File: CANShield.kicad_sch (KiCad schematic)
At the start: 25 parts, among them J1 Conn_01x04_Socket, J2 Conn_02x19_Odd_Even, J3 Conn_02x19_Odd_Even, U1 TJA1443ATK/0Z

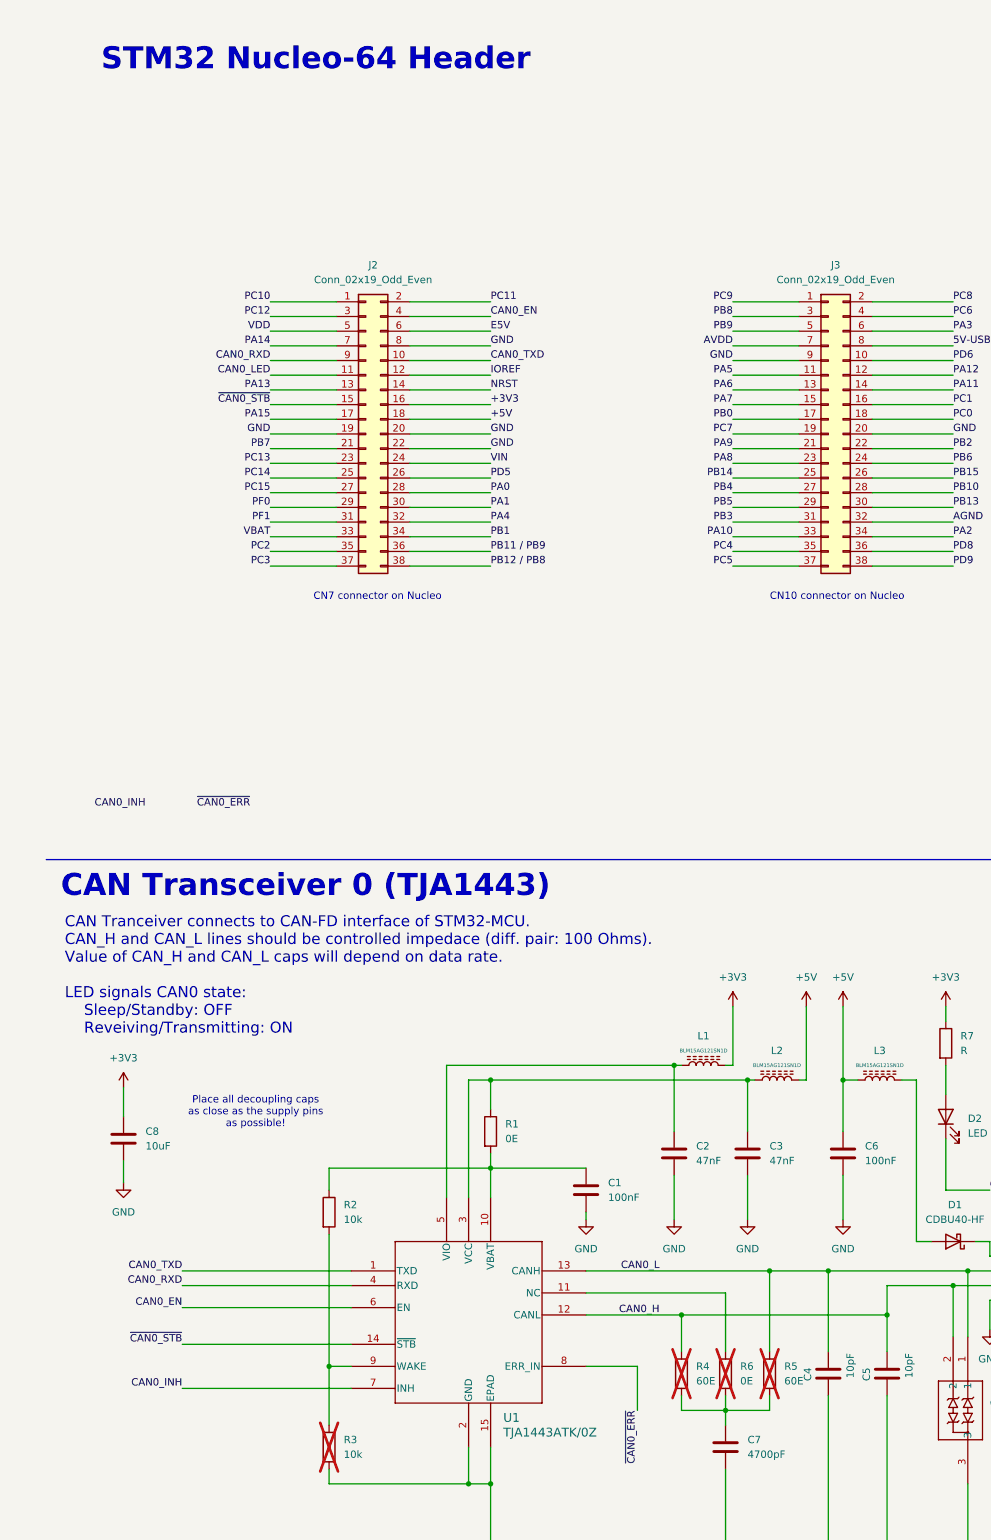
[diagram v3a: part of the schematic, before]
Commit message: Update CANShield.kicad_sch
Add testpoints and documentation
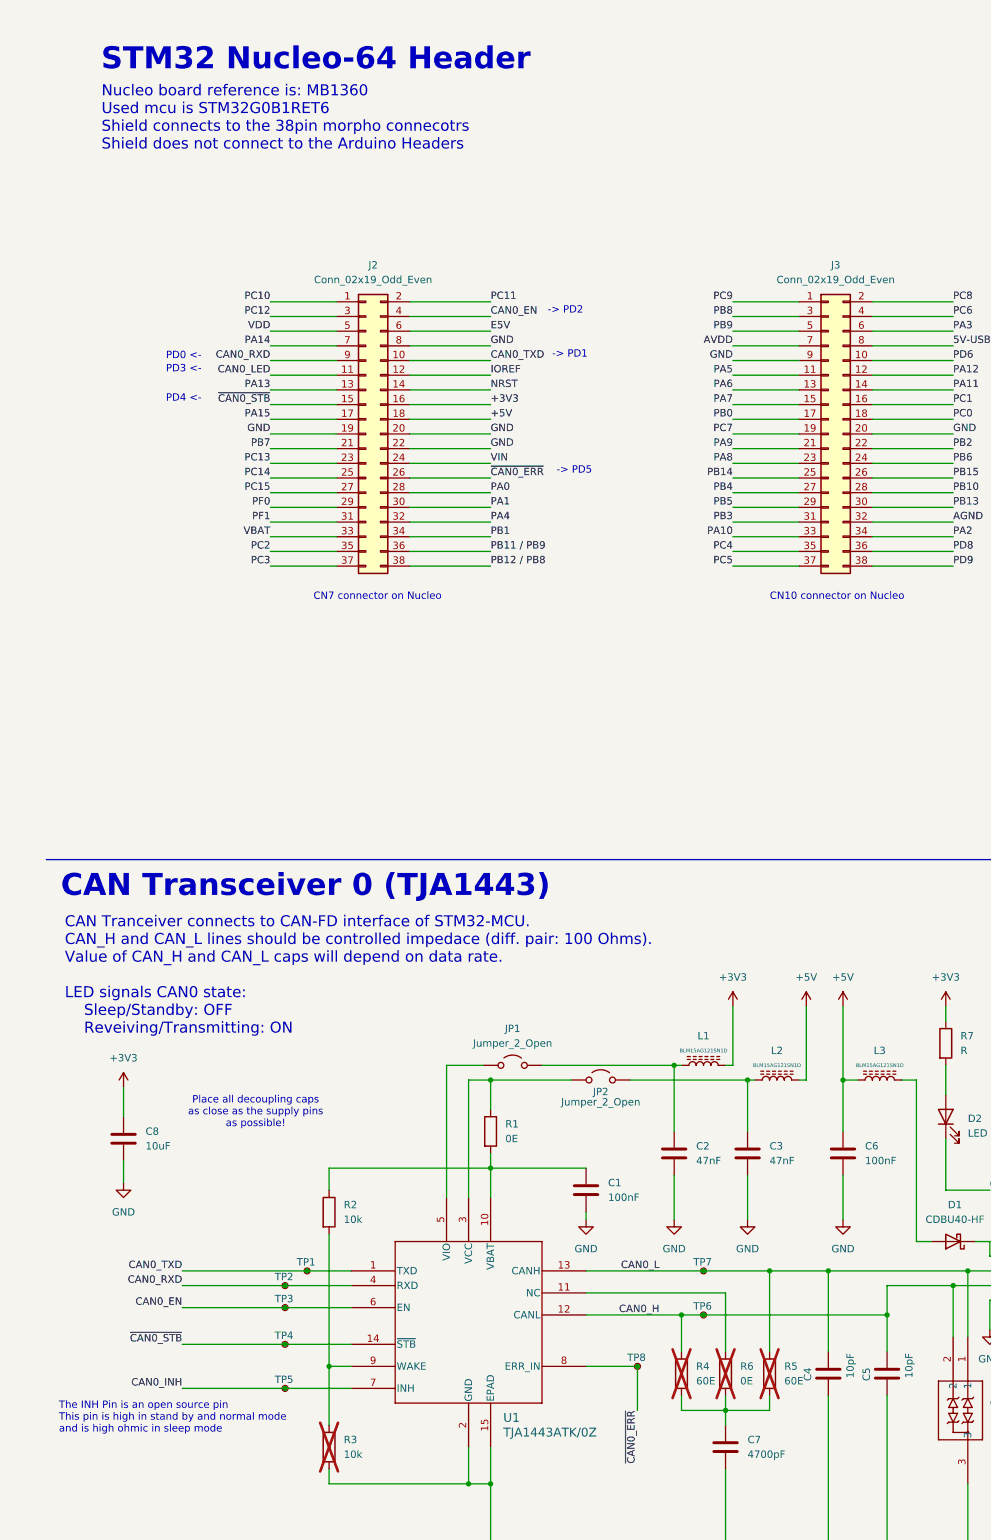
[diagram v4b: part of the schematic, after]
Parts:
- added JP1, JP2: Jumper_2_Open, symbol Jumper:Jumper_2_Open
- added TP1, TP2, TP3, TP4, TP5, TP6, TP7, TP8: TestPoint_Small, symbol Connector:TestPoint_Small
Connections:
- net PD5 is gone; now on net ~{CAN0_ERR}: J2.26 (Pin_26)
- net CAN0_EN: now also TP3.1
- net CAN0_H: now also TP6.1
- net CAN0_INH: now also TP5.1
- net CAN0_L: now also TP7.1
- net CAN0_RXD: now also TP2.1
- net CAN0_TXD: now also TP1.1
- net ~{CAN0_ERR}: now also TP8.1
- net ~{CAN0_STB}: now also TP4.1
- net at R1.1, U1.3 (VCC): now also JP2.1 (A); no longer C3.1, L2.1
- net at C2.1, L1.1: now also JP1.2 (B); no longer U1.5 (VIO)
- new net: JP1.1 (A), U1.5 (VIO)
- new net: C3.1, JP2.2 (B), L2.1
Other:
- note added: "-> PD1"
- note added: "-> PD2"
- note added: "-> PD5"
- note added: "Nucleo board reference is: MB1360 Used mcu is STM32G0B1RET6 Shield connects to the 38pin morpho connecotrs Shield does not connect to the Arduino Headers"
- note added: "PD0 <-"
- note added: "PD3 <-"
- note added: "PD4 <-"
- note added: "The INH Pin is an open source pin This pin is high in stand by and normal mode and is high ohmic in sleep mode"

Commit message: Update CANShield.kicad_sch
Add probe connector and Flash memory
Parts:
- added C10: 120uF, symbol Device:C
- added C11, C13: 100nF, symbol Device:C
- added C12, C9: 10uF, symbol Device:C
- added CR2: PESD2CANFD27V-TR, SOT23_PESD2_NEX, symbol PESD2CANFD27V:PESD2CANFD27V-TR
- added D3: LED_ARGB, symbol Device:LED_ARGB
- added J4: Conn_01x06_Socket, symbol Connector:Conn_01x06_Socket
- added L4, L5, L6, L7: BLM15AG121SN1D, symbol Device:L_Ferrite
- added Q1, Q2, Q3: Si1308EDL, Package_TO_SOT_SMD:SOT-323_SC-70, symbol Transistor_FET:Si1308EDL
- added R10, R14, R15, R16, R17, R18, R19, R20, R8, R9: 100k, symbol Device:R
- added R11, R12, R13: 1k, symbol Device:R
- added U2: AT25SF081-XMHD-X, Package_SO:TSSOP-8_4.4x3mm_P0.65mm, symbol Memory_Flash:AT25SF081-XMHD-X
- added U5: BD2222G, Package_SO:TSOP-6_1.65x3.05mm_P0.95mm, symbol Power_Management:BD2222G
- R7: value R -> 1k
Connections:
- net +3V3: now also C12.1, C13.1, D3.1 (A), R17.1, R19.1, R20.1, U2.8 (VCC)
- net +5V: now also C9.1, U5.1 (IN)
- net GND: now also C10.2, C11.2, C12.2, C13.2, C9.2, CR2.3, L6.1, Q1.2 (S), Q2.2 (S), Q3.2 (S), R10.2, R16.2, R18.2, R8.2, R9.2, U2.4 (GND), U5.2 (GND)
- net PA10 renamed PROBE_EN
- net PROBE_EN: now also R16.1, U5.3 (EN)
- net PA8 renamed FLASH_CS
- net FLASH_CS: now also R19.2, U2.1 (~{CS})
- net PA9 renamed ~{WP}
- net ~{WP}: now also U2.3 (~{WP}/IO2)
- net PB13 renamed SCLK
- net SCLK: now also U2.6 (SCK)
- net PB14 renamed MISO
- net MISO: now also U2.2 (SO/IO1)
- net PB15 renamed MOSI
- net MOSI: now also U2.5 (SI/IO0)
- net PB3 renamed LED0_RED
- net LED0_RED: now also Q1.1 (G), R8.1
- net PB4 renamed LED0_BLU
- net LED0_BLU: now also Q3.1 (G), R10.1
- net PB5 renamed LED0_GRN
- net LED0_GRN: now also Q2.1 (G), R9.1
- net PC4 renamed USART1_TX
- net USART1_TX: now also CR2.1, L4.1, R15.2
- net PC5 renamed USART1_RX
- net USART1_RX: now also CR2.2, L5.1, R14.2
- net PD9 renamed ~{PRB_FLG}
- net ~{PRB_FLG}: now also R17.2, U5.4 (~{OC})
- new net: R18.1, U5.5 (ILIM)
- new net: Q2.3 (D), R12.2
- new net: D3.2 (RK), R11.2
- new net: D3.3 (GK), R12.1
- new net: D3.4 (BK), R13.1
- new net: J4.2 (Pin_2), L6.2
- new net: Q3.3 (D), R13.2
- new net: J4.1 (Pin_1), L7.2
- new net: Q1.3 (D), R11.1
- new net: J4.4 (Pin_4), L4.2
- new net: J4.3 (Pin_3), L5.2
- new net PVCC: C10.1, C11.1, L7.1, R14.1, R15.1, U5.6 (OUT)
- new net ~{HOLD}: R20.2, U2.7 (~{HOLD}/IO3)
- no-connect marks 0 -> 2
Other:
- note added: "-> PB13"
- note added: "-> PB15"
- note added: "-> PD9"
- note added: "8Mbit NOR-Flash Memory to save firmware update"
- note added: "Current limiting probe switch. Probe connector with ESD protection."
- note added: "Flash Memory"
- note added: "LED States: RED: Fatal Error Yellow: In progress Green: Progress successful Magenta: Service Mode Cyan: Open state"
- note added: "PA10 <-"
- note added: "PA8 <-"
- note added: "PA9 <-"
- note added: "PB14 <-"
- note added: "PB3 <-"
- note added: "PB4 <-"
- note added: "PB5 <-"
- note added: "PC4 <-"
- note added: "PC5 <-"
- note added: "Probe Switch"
- note added: "RGB Status LED indicates device state. In Canable Dongle this will be the LED Ring indication"
- note added: "Status indication"

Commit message: Update CANShield.kicad_sch
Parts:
- added C114: 100nF, Capacitor_SMD:C_0402_1005Metric_Pad0.74x0.62mm_HandSolder, symbol Device:C
- added D104: LED_ARGB, 155124M173200:LED_155124M173200, symbol Device:LED_ARGB
- added FID101, FID102, FID103: Fiducial, Fiducial:Fiducial_0.75mm_Mask2.25mm, symbol Mechanical:Fiducial
- added H101, H102, H103: MountingHole, MountingHole:MountingHole_2.7mm_M2.5, symbol Mechanical:MountingHole
- added JP102, JP103: SolderJumper_2_Open, Connector_PinHeader_2.54mm:PinHeader_1x02_P2.54mm_Vertical, symbol Jumper:SolderJumper_2_Open
- added R118, R119, R124, R125, R126: 0E, Resistor_SMD:R_0402_1005Metric_Pad0.72x0.64mm_HandSolder, symbol Device:R
- added R122: 100k, Resistor_SMD:R_0402_1005Metric_Pad0.72x0.64mm_HandSolder, symbol Device:R
- added TP109, TP110, TP111, TP112, TP113, TP114, TP115, TP116, TP117, TP118: TestPoint_Small, TestPoint:TestPoint_Pad_D1.0mm, symbol Connector:TestPoint_Small
- added U104: MR20H40, Package_SO:SOIC-8-1EP_3.9x4.9mm_P1.27mm_EP2.29x3mm, symbol Memory_NVRAM:MR20H40
- C101: renamed from C8; footprint (none) -> Capacitor_SMD:C_0603_1608Metric_Pad1.08x0.95mm_HandSolder
- C102: renamed from C1; footprint (none) -> Capacitor_SMD:C_0402_1005Metric_Pad0.74x0.62mm_HandSolder
- C103: renamed from C2; footprint (none) -> Capacitor_SMD:C_0402_1005Metric_Pad0.74x0.62mm_HandSolder
- C104: renamed from C7; footprint (none) -> Capacitor_SMD:C_0402_1005Metric_Pad0.74x0.62mm_HandSolder
- C105: renamed from C3; footprint (none) -> Capacitor_SMD:C_0402_1005Metric_Pad0.74x0.62mm_HandSolder
- C106: renamed from C4; footprint (none) -> Capacitor_SMD:C_0402_1005Metric_Pad0.74x0.62mm_HandSolder
- C107: renamed from C6; footprint (none) -> Capacitor_SMD:C_0402_1005Metric_Pad0.74x0.62mm_HandSolder
- C108: renamed from C5; footprint (none) -> Capacitor_SMD:C_0402_1005Metric_Pad0.74x0.62mm_HandSolder
- C109: renamed from C12; footprint (none) -> Capacitor_SMD:C_0603_1608Metric_Pad1.08x0.95mm_HandSolder
- C110: renamed from C9; footprint (none) -> Capacitor_SMD:C_0603_1608Metric_Pad1.08x0.95mm_HandSolder
- C111: renamed from C13; footprint (none) -> Capacitor_SMD:C_0402_1005Metric_Pad0.74x0.62mm_HandSolder
- C112: renamed from C10; footprint (none) -> Capacitor_SMD:C_0603_1608Metric_Pad1.08x0.95mm_HandSolder
- C113: renamed from C11; footprint (none) -> Capacitor_SMD:C_0402_1005Metric_Pad0.74x0.62mm_HandSolder
- CR101: renamed from CR1; footprint SOT23_PESD2_NEX -> PESD2CANFD27V-TR:SOT23_PESD2_NEX
- CR102: renamed from CR2; footprint SOT23_PESD2_NEX -> PESD2CANFD27V-TR:SOT23_PESD2_NEX
- D101: renamed from D2; footprint (none) -> LED_SMD:LED_0402_1005Metric_Pad0.77x0.64mm_HandSolder
- D103: renamed from D3; footprint (none) -> 155124M173200:LED_155124M173200
- J101: renamed from J2; footprint (none) -> Connector_PinHeader_2.54mm:PinHeader_2x19_P2.54mm_Vertical
- J102: renamed from J3; footprint (none) -> Connector_PinHeader_2.54mm:PinHeader_2x19_P2.54mm_Vertical
- J103: renamed from J1; footprint (none) -> Connector_PinHeader_2.54mm:PinHeader_1x04_P2.54mm_Horizontal
- J104: renamed from J4; footprint (none) -> Connector_Molex:Molex_PicoBlade_53048-0610_1x06_P1.25mm_Horizontal
- JP101: renamed from JP1; footprint (none) -> Connector_PinHeader_2.54mm:PinHeader_1x02_P2.54mm_Vertical
- JP104: renamed from JP2; footprint (none) -> Connector_PinHeader_2.54mm:PinHeader_1x02_P2.54mm_Vertical
- L101: renamed from L1; footprint (none) -> Inductor_SMD:L_0402_1005Metric_Pad0.77x0.64mm_HandSolder
- L102: renamed from L2; footprint (none) -> Inductor_SMD:L_0402_1005Metric_Pad0.77x0.64mm_HandSolder
- L103: renamed from L3; footprint (none) -> Inductor_SMD:L_0402_1005Metric_Pad0.77x0.64mm_HandSolder
- L104: renamed from L7; footprint (none) -> Inductor_SMD:L_0402_1005Metric_Pad0.77x0.64mm_HandSolder
- L105: renamed from L6; footprint (none) -> Inductor_SMD:L_0402_1005Metric_Pad0.77x0.64mm_HandSolder
- L106: renamed from L5; footprint (none) -> Inductor_SMD:L_0402_1005Metric_Pad0.77x0.64mm_HandSolder
- L107: renamed from L4; footprint (none) -> Inductor_SMD:L_0402_1005Metric_Pad0.77x0.64mm_HandSolder
- R101: renamed from R2; footprint (none) -> Resistor_SMD:R_0402_1005Metric_Pad0.72x0.64mm_HandSolder
- R102: renamed from R3; footprint (none) -> Resistor_SMD:R_0402_1005Metric_Pad0.72x0.64mm_HandSolder
- R103: renamed from R1; footprint (none) -> Resistor_SMD:R_0402_1005Metric_Pad0.72x0.64mm_HandSolder
- R104: renamed from R4; footprint (none) -> Resistor_SMD:R_0603_1608Metric_Pad0.98x0.95mm_HandSolder
- R105: renamed from R6; footprint (none) -> Resistor_SMD:R_0603_1608Metric_Pad0.98x0.95mm_HandSolder
- R106: renamed from R5; footprint (none) -> Resistor_SMD:R_0603_1608Metric_Pad0.98x0.95mm_HandSolder
- R107: renamed from R7; footprint (none) -> Resistor_SMD:R_0402_1005Metric_Pad0.72x0.64mm_HandSolder
- R108: renamed from R16; footprint (none) -> Resistor_SMD:R_0402_1005Metric_Pad0.72x0.64mm_HandSolder
- R109: renamed from R8; footprint (none) -> Resistor_SMD:R_0402_1005Metric_Pad0.72x0.64mm_HandSolder
- R110: renamed from R11; footprint (none) -> Resistor_SMD:R_0402_1005Metric_Pad0.72x0.64mm_HandSolder
- R111: renamed from R17; footprint (none) -> Resistor_SMD:R_0402_1005Metric_Pad0.72x0.64mm_HandSolder
- R112: renamed from R19; footprint (none) -> Resistor_SMD:R_0402_1005Metric_Pad0.72x0.64mm_HandSolder
- R113: renamed from R18; footprint (none) -> Resistor_SMD:R_0402_1005Metric_Pad0.72x0.64mm_HandSolder
- R114: renamed from R9; footprint (none) -> Resistor_SMD:R_0402_1005Metric_Pad0.72x0.64mm_HandSolder
- R115: renamed from R20; footprint (none) -> Resistor_SMD:R_0402_1005Metric_Pad0.72x0.64mm_HandSolder
- R116: renamed from R12; footprint (none) -> Resistor_SMD:R_0402_1005Metric_Pad0.72x0.64mm_HandSolder
- R117: renamed from R15; footprint (none) -> Resistor_SMD:R_0402_1005Metric_Pad0.72x0.64mm_HandSolder
- R120: renamed from R10; footprint (none) -> Resistor_SMD:R_0402_1005Metric_Pad0.72x0.64mm_HandSolder
- R121: renamed from R14; footprint (none) -> Resistor_SMD:R_0402_1005Metric_Pad0.72x0.64mm_HandSolder
- R123: renamed from R13; footprint (none) -> Resistor_SMD:R_0402_1005Metric_Pad0.72x0.64mm_HandSolder
- TP101: renamed from TP2; footprint (none) -> TestPoint:TestPoint_Pad_D1.0mm
- TP102: renamed from TP3; footprint (none) -> TestPoint:TestPoint_Pad_D1.0mm
- TP103: renamed from TP4; footprint (none) -> TestPoint:TestPoint_Pad_D1.0mm
- TP104: renamed from TP5; footprint (none) -> TestPoint:TestPoint_Pad_D1.0mm
- TP105: renamed from TP1; footprint (none) -> TestPoint:TestPoint_Pad_D1.0mm
- TP106: renamed from TP8; footprint (none) -> TestPoint:TestPoint_Pad_D1.0mm
- TP107: renamed from TP7; footprint (none) -> TestPoint:TestPoint_Pad_D1.0mm
- TP108: renamed from TP6; footprint (none) -> TestPoint:TestPoint_Pad_D1.0mm
- U101: renamed from U1; footprint HVSON14_SOT1086-2_NXP -> TJA1443ATK:HVSON14_SOT1086-2_NXP
- renumbered D1 to D102, Q1 to Q101, Q2 to Q102, Q3 to Q103, U5 to U102, U2 to U103
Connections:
- net +3V3: now also C114.1, D104.1 (A), JP102.1 (A), JP102.2 (B), R122.2, TP114.1, U104.8 (VDD)
- net +5V: now also JP103.1 (A), JP103.2 (B)
- net FLASH_CS: now also R119.1, TP109.1
- net GND: now also C114.2, U104.4 (VSS), U104.9 (PAD)
- net MISO: now also R125.1, TP112.1
- net MOSI: now also R126.1, TP111.1
- net PC13: now also TP116.1
- net PC14: now also TP117.1
- net PC15: now also TP118.1
- net PROBE_EN: now also TP115.1
- net SCLK: now also R124.1, TP110.1
- net ~{WP}: now also R118.1, TP113.1
- net at D103.2 (RK), R110.2: now also D104.2 (RK)
- net at D103.3 (GK), R116.1: now also D104.3 (GK)
- net at D103.4 (BK), R123.1: now also D104.4 (BK)
- new net: R126.2, U104.5 (SI)
- new net: R119.2, U104.1 (~{CS})
- new net: R125.2, U104.2 (SO)
- new net: R118.2, U104.3 (~{WP})
- new net: R124.2, U104.6 (SCK)
- new net: R122.1, U104.7 (~{HOLD})
- no-connect marks 2 -> 52
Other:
- note added: "8Mbit NOR-Flash Memory to save firmware update Optional: 4MB SDRAM to save firmware for firmware update"
- note added: "Fiduclials and mounting holes"
- note added: "IS66WVS4M8BLL-104NLI-TR Optional: IS66WVS1M8BLL-104NLI-TR"
- note removed: "8Mbit NOR-Flash Memory to save firmware update"
- moved on the sheet: Q102, Q103, R109, R114, R116, R120, R123

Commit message: Add PCB
started design
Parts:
- J101, J102: footprint Connector_PinHeader_2.54mm:PinHeader_2x19_P2.54mm_Vertical -> Connector_PinSocket_2.54mm:PinSocket_2x19_P2.54mm_Vertical
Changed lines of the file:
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@@
 			)
 		)
-		(property "Footprint" "Connector_PinHeader_2.54mm:PinHeader_2x19_P2.54mm_Vertical"
+		(property "Footprint" "Connector_PinSocket_2.54mm:PinSocket_2x19_P2.54mm_Vertical"
 			(at 147.32 85.09 0)
 			(effects
@@
 			)
 		)
-		(property "Footprint" "Connector_PinHeader_2.54mm:PinHeader_2x19_P2.54mm_Vertical"
+		(property "Footprint" "Connector_PinSocket_2.54mm:PinSocket_2x19_P2.54mm_Vertical"
 			(at 67.31 85.09 0)
 			(effects
